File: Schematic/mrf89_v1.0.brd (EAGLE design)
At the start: 27.9 x 41.6 mm, 20 parts, among them Q1 FC-12M, U1 MSP430FR5969, U5 MRF89XAM8A

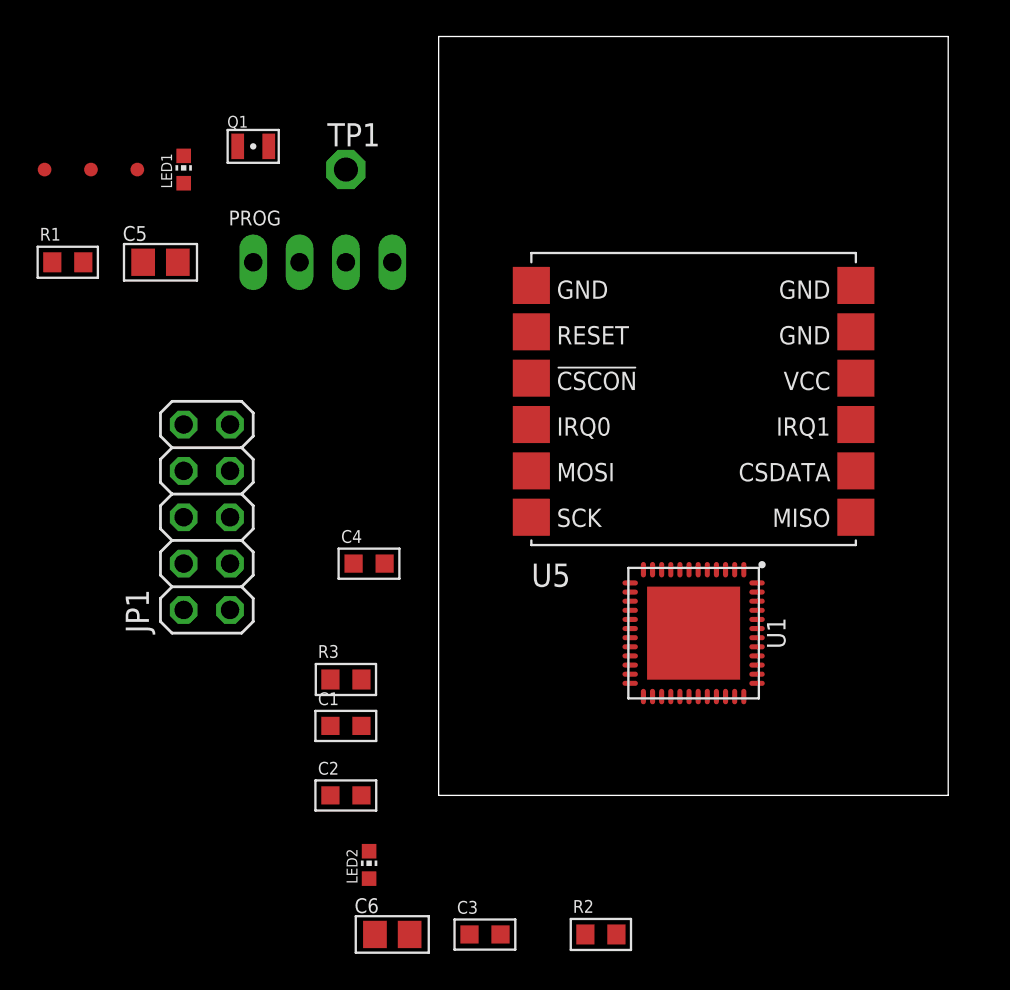
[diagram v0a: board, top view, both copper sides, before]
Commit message: Finalized version 1.0
Finalized version of schematic and PCB.
Version 1.0
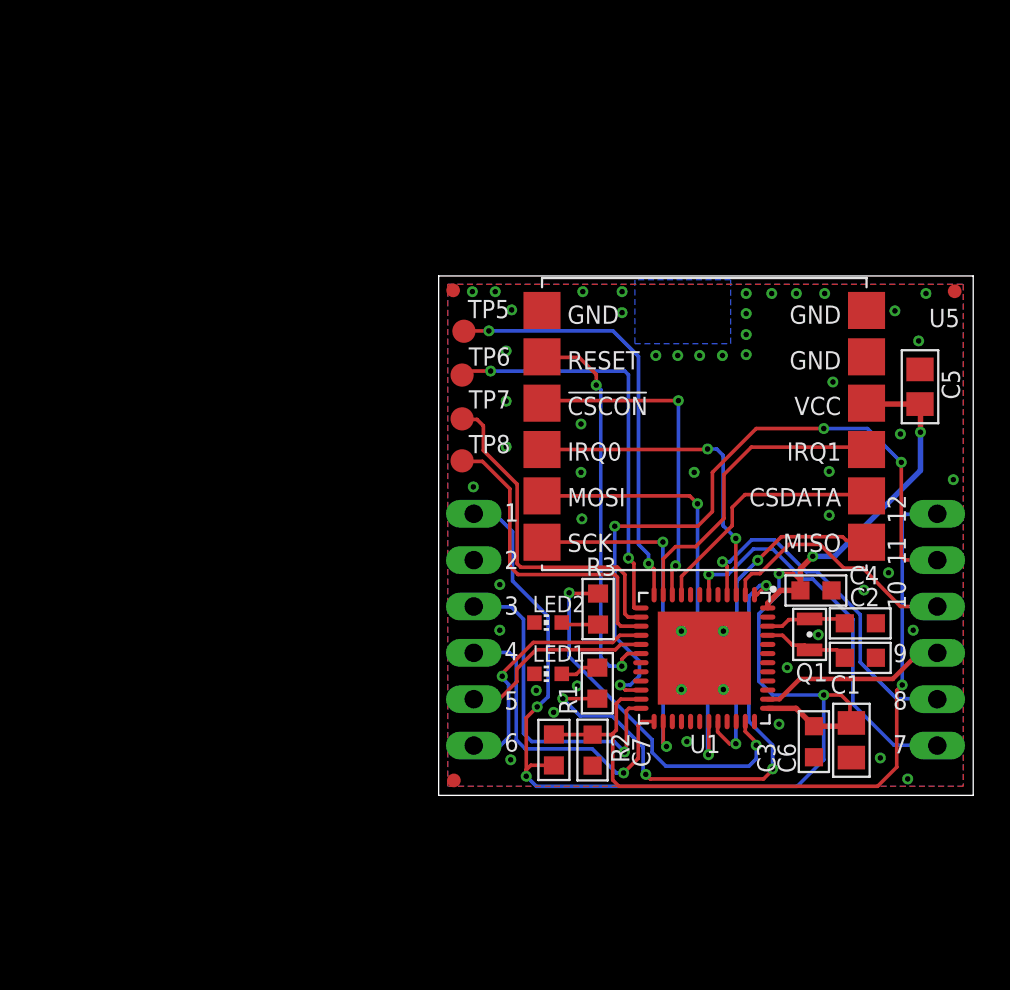
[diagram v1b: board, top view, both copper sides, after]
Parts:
- removed PROG: (no value), pinhead:1X04
- removed TP1: PTR1PAD1-13, testpad:P1-13
- added C7: 1nF, rcl:C0603
- added JP2: RIGHT, pinhead:1X06
- added TP5, TP6, TP7, TP8: TPB1,27, testpad:B1,27
- JP1: value TC2050-Series -> LEFT; device pinhead:2X05 -> pinhead:1X06
- moved FID1 45.3 mm to (28.3, 27.6)
- moved C5 42.2 mm to (26.4, 22.4), turned to 90 degrees
- moved Q1 40.6 mm to (20.3, 8.82), turned to 90 degrees
- moved FID2 38.9 mm to (0.83, 0.82)
- moved R1 37.1 mm to (8.70, 6.15), turned to 270 degrees
- moved LED1 34.1 mm to (6.00, 6.66), turned to 90 degrees
- moved C2 29.7 mm to (23.1, 9.43)
- moved C1 28.4 mm to (23.1, 7.54)
- moved C6 27.3 mm to (22.6, 3.02), turned to 270 degrees
- moved C4 24.5 mm to (20.7, 11.2)
- moved FID3 23.3 mm to (0.80, 27.7)
- moved C3 20.9 mm to (20.6, 2.94), turned to 270 degrees
- moved LED2 16.5 mm to (6.00, 9.47), turned to 90 degrees
- moved JP1 15.9 mm to (1.92, 9.08)
- moved R3 14.3 mm to (8.73, 10.2), turned to 270 degrees
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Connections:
- net N$1 renamed LFXIN
- net N$16 renamed P1.0
- net N$2 renamed LFXOUT
- net N$4 renamed P4.6
- removed net !RST: JP1.2
- removed net (NC): JP1.10
- removed net DBG_UART_RXD: U1.21
- removed net DBG_UART_TXD: U1.20
- removed net MRF89_!RST: U1.18
- removed net PRG_!RST: PROG.2
- removed net PRG_TEST: PROG.3
- removed net VCC_IN: JP1.7
- removed net VCC_OUT: JP1.3
- net 3V3: now also JP1.6; no longer PROG.4
- net GND: now also C7.2, JP1.5; no longer JP1.4, PROG.1
- net GPIO_P1.1: now also JP2.4
- net GPIO_P2.7: now also JP2.3
- net GPIO_P3.0: now also JP2.2
- net GPIO_P3.2: now also JP2.1
- net MRF_!RST: now also U1.18
- net RST: now also C7.1, JP2.6
- net TCK: now also TP8.TP; no longer JP1.8
- net TDI: now also TP6.TP; no longer JP1.5
- net TDO: now also TP5.TP; no longer JP1.1
- net TEST: now also JP2.5; no longer JP1.6
- net TMS: now also TP7.TP; no longer JP1.9
- net UART_CTS: now also JP1.1
- net UART_RTS: now also JP1.2
- net UART_RX: now also JP1.4
- net UART_TX: now also JP1.3
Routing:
- net 3V3: track 0.00 -> 78.2 mm, vias 0 -> 6
- net RST: track 0.00 -> 40.9 mm, vias 0 -> 1
- net TEST: track 0.00 -> 38.4 mm, vias 0 -> 4
- net P1.0: track 0.00 -> 28.3 mm, vias 0 -> 4
- net SPI_MOSI: track 0.00 -> 24.5 mm, vias 0 -> 2
- net TDO: track 0.00 -> 23.6 mm, vias 0 -> 2
- net TDI: track 0.00 -> 22.6 mm, vias 0 -> 2
- net MRF_!RST: track 0.00 -> 21.9 mm, vias 0 -> 2
- net GPIO_P3.2: track 0.00 -> 21.4 mm, vias 0 -> 1
- net P4.6: track 0.00 -> 20.7 mm, vias 0 -> 2
- net SPI_CLK: track 0.00 -> 19.4 mm, vias 0 -> 2
- net GPIO_P3.0: track 0.00 -> 19.3 mm, vias 0 -> 1
- net SPI_MISO: track 0.00 -> 19.0 mm, vias 0 -> 2
- net TMS: track 0.00 -> 18.9 mm
- net UART_RX: track 0.00 -> 18.4 mm, vias 0 -> 1
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- added copper zone on layer 1, net GND
- added copper zone on layer 16, net GND
- added copper zone on layer 16, net N$1
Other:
- board size 27.9 x 41.6 mm -> 29.3 x 28.5 mm
- board text added: "1"
- board text added: "10"
- board text added: "11"
- board text added: "12"
- board text added: "2"
- board text added: "3"
- board text added: "4"
- board text added: "5"
- board text added: "6"
- board text added: "7"
- board text added: "8"
- board text added: "9"
- board text added: "CTS"
- board text added: "GND"
- board text added: "MIRA_AT_868/915MHz v1.0"
- board text added: "P1.1"
- board text added: "P2.7"
- board text added: "P3.0"
- board text added: "P3.2"
- board text added: "RST"
- board text added: "RTS"
- board text added: "RX"
- board text added: "TEST"
- board text added: "TX"
- board text added: "VCC"
